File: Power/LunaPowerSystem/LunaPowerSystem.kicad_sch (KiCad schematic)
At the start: 6 parts, among them SW1 KILL_SWITCH

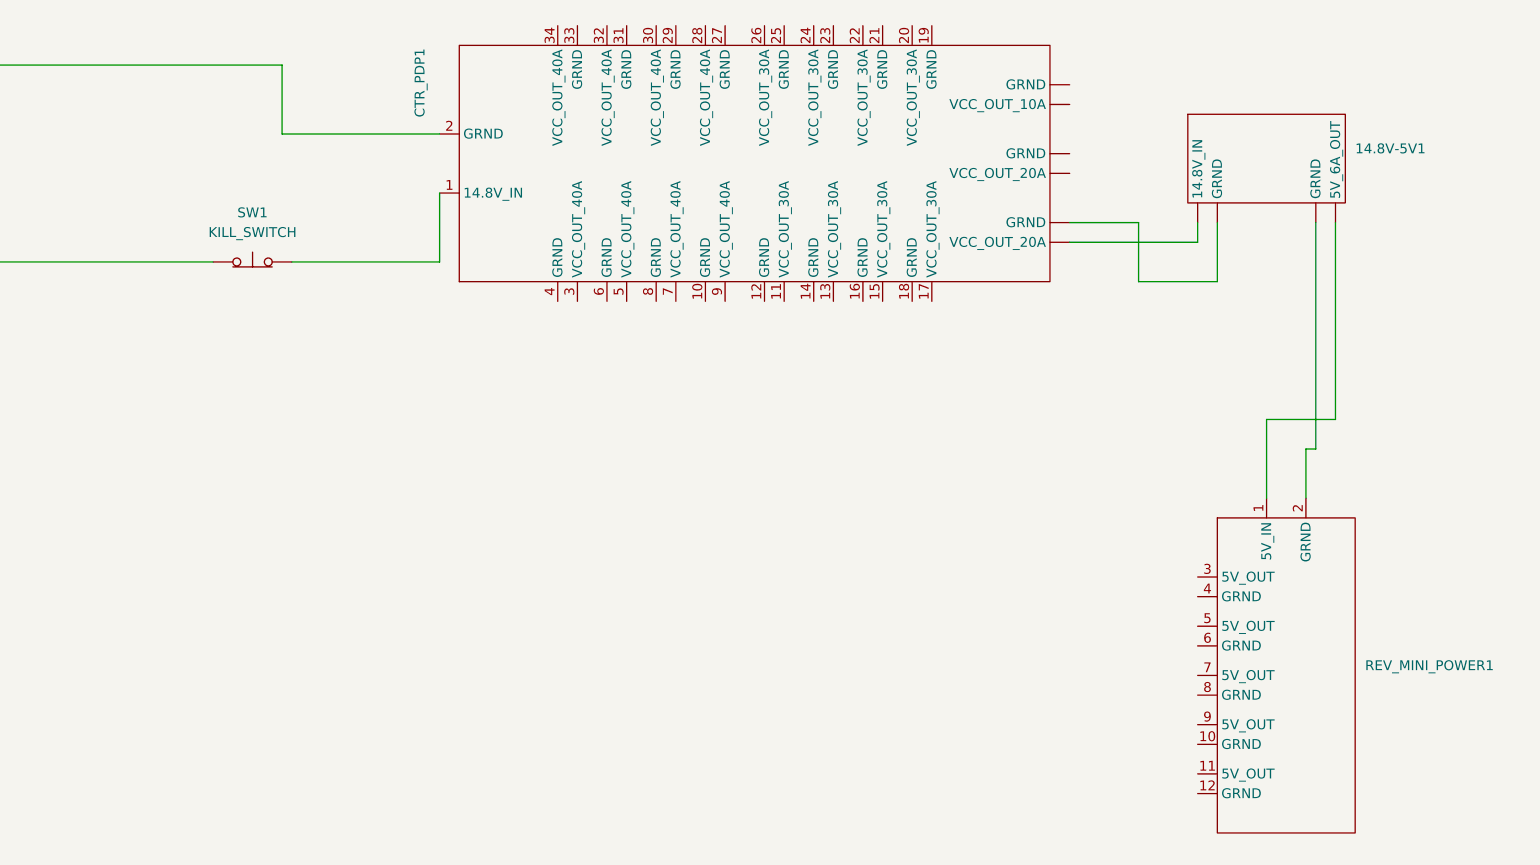
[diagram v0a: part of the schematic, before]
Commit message: Fixed things
At least my version of the mech schematic was broken, so I copied in the last version committed by Alex, and I updated the power schematic to use library symbols
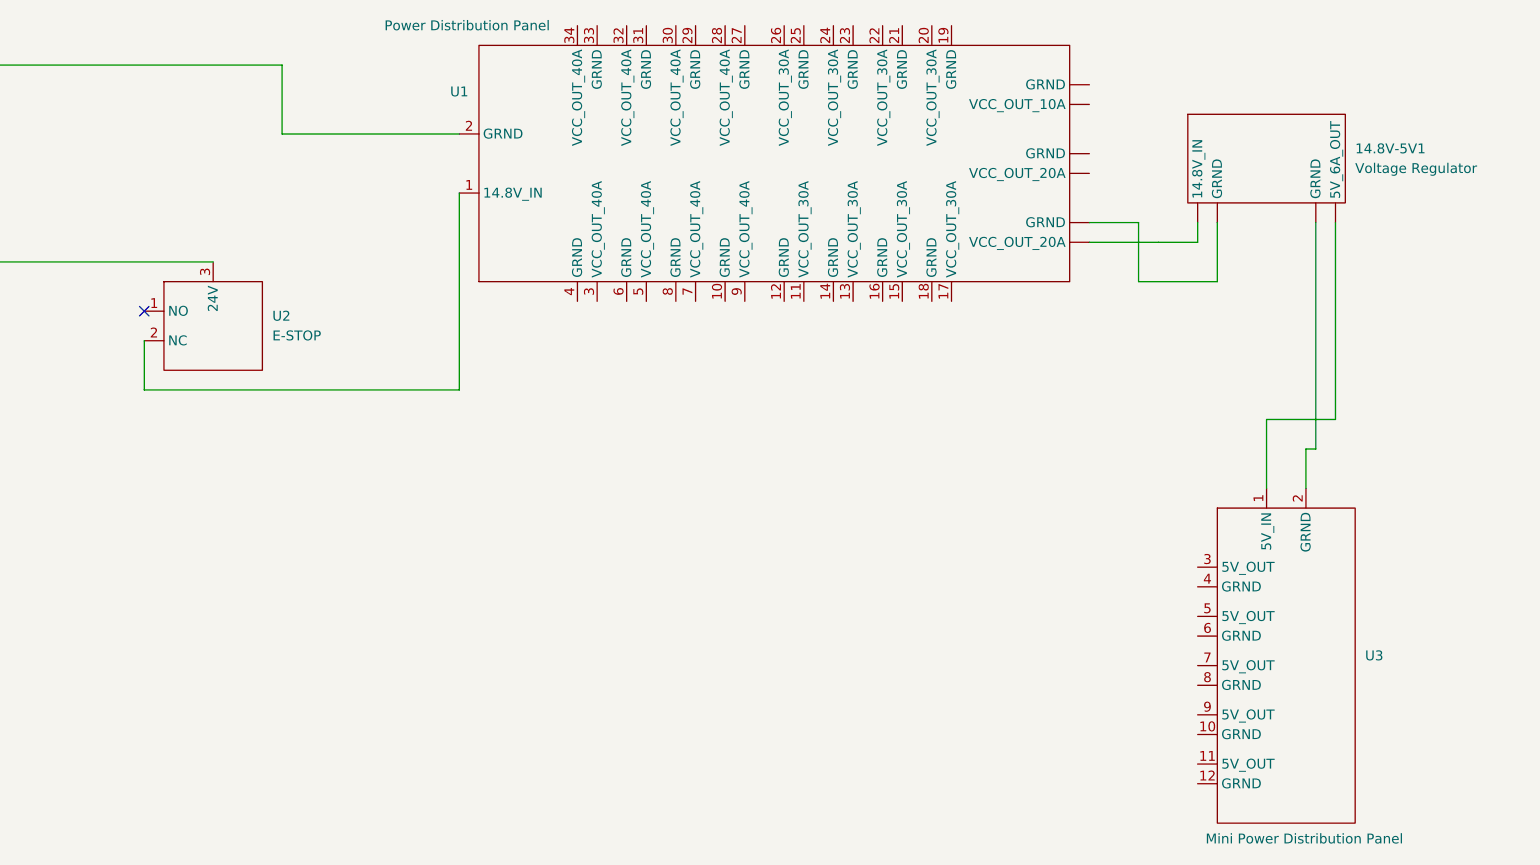
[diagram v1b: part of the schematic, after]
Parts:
- removed CTR_PDP1: ~, symbol New_Library:CTR_PDP
- removed REV_MINI_POWER1: ~, symbol New_Library:REV_Mini_Power_Module
- removed SW1: KILL_SWITCH, symbol Switch:SW_Push_Open
- added U1: Power Distribution Panel, symbol Lunabotics 2025-26:Power_Distribution_Panel
- added U2: E-STOP, symbol Lunabotics 2025-26:A22E-M-11
- added U3: Mini Power Distribution Panel, symbol Lunabotics 2025-26:Mini_Power_Distribution_Panel
- 14.8V-5V1: value ~ -> Voltage Regulator
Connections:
- net at BT1.1 (+), BT2.1 (+): now also U2.3 (24V)
- net at BT1.2 (-), BT2.2 (-): now also U1.2 (GRND)
- net at 14.8V-5V1. (5V_6A_OUT): now also U3.2 (GRND)
- new net: 14.8V-5V1. (5V_6A_OUT), U1. (GRND) (x2)
- new net: U1.1 (14.8V_IN), U2.2 (NC)
- new net: 14.8V-5V1. (5V_6A_OUT), U3.1 (5V_IN)
- no-connect marks 0 -> 1

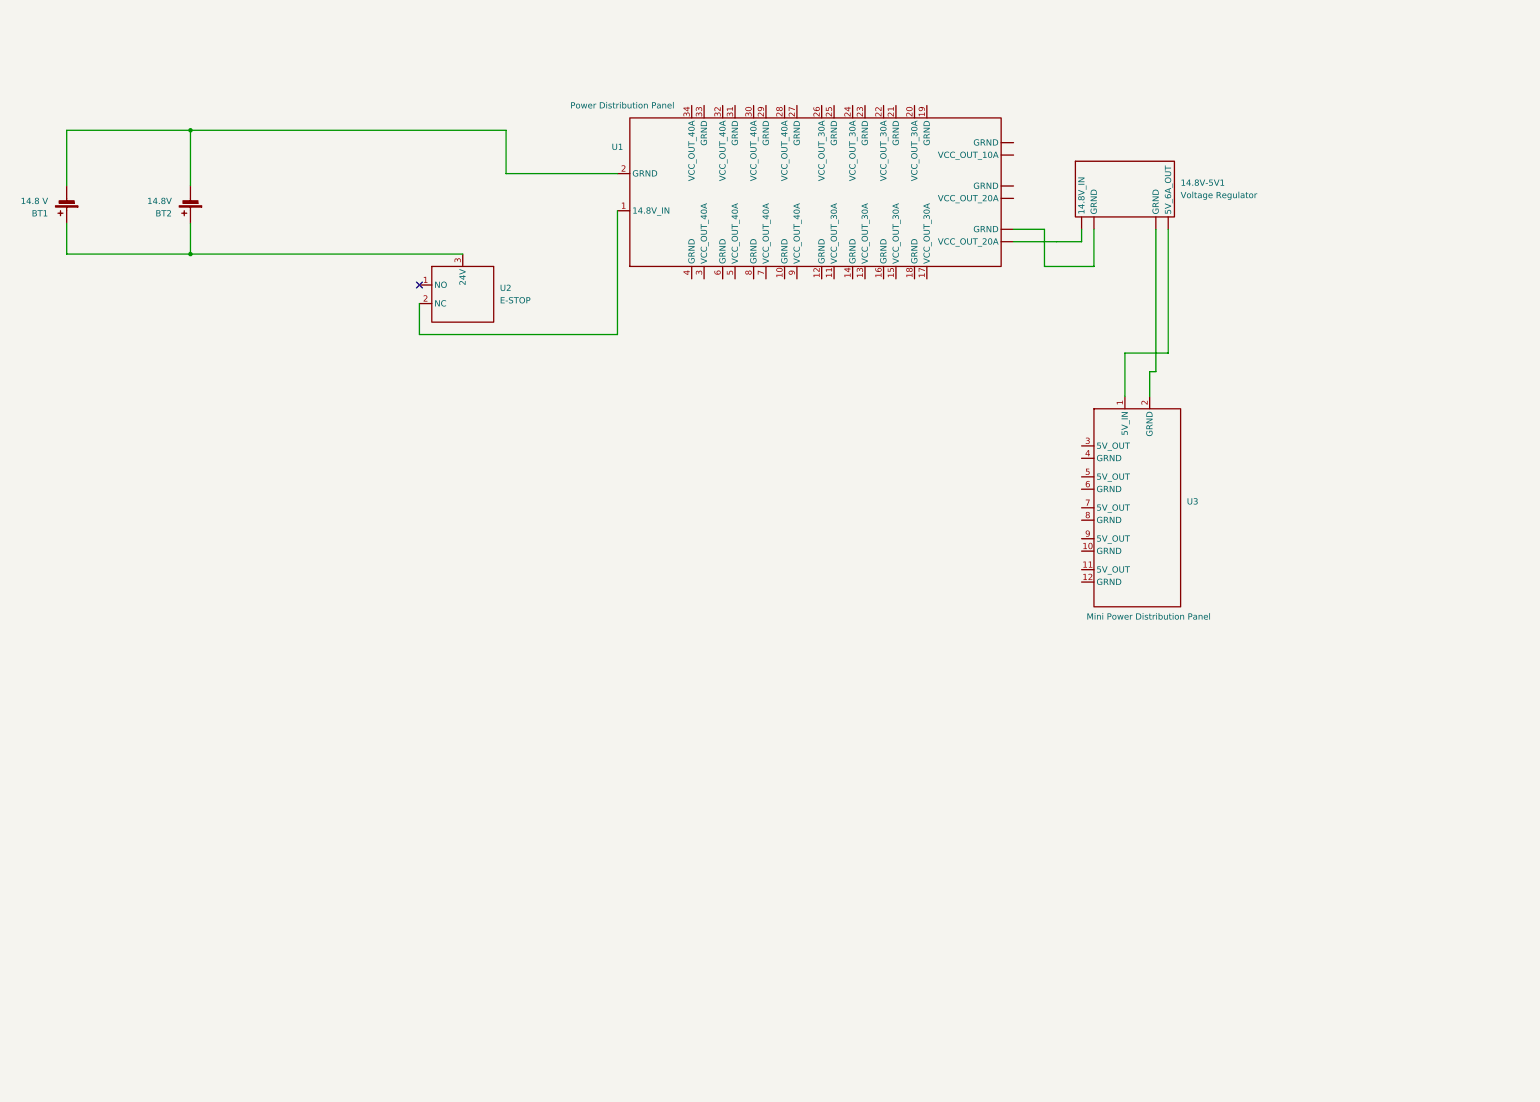
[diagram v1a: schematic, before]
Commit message: Completed Schematics
Only thing not included is a linear actuator and motor controller. Waiting on Mechanical to give us what they want to use
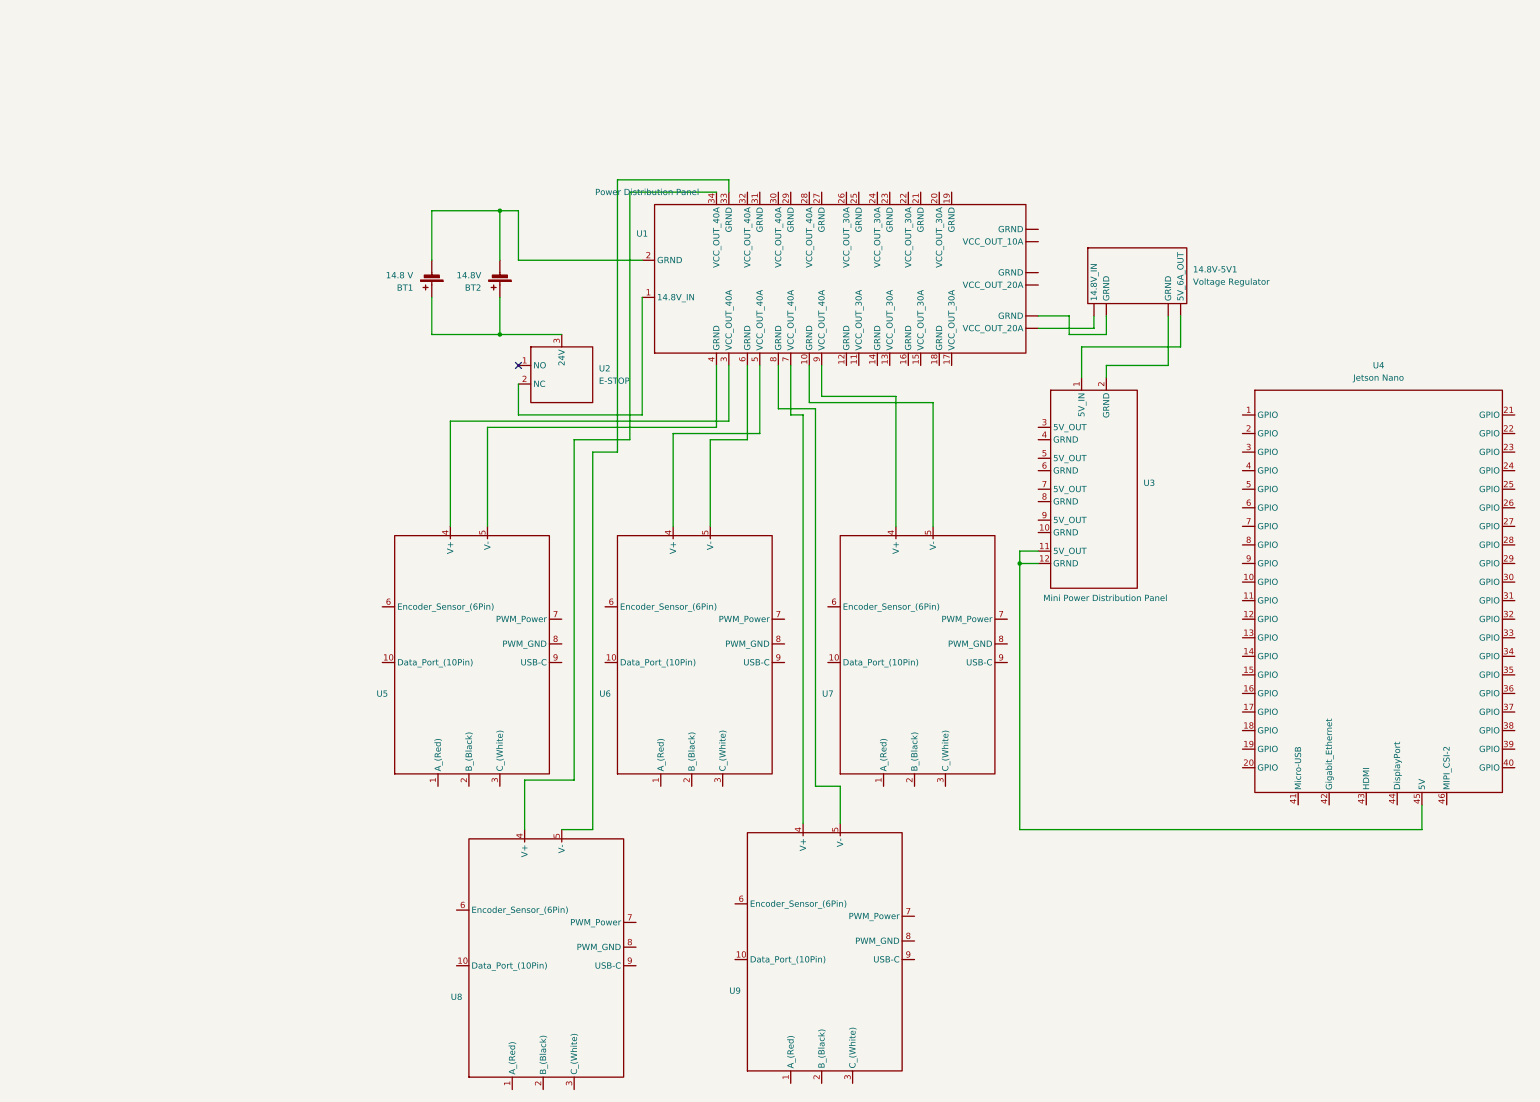
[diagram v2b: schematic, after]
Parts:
- added U4: Jetson Nano, symbol Lunabotics 2025-26:Jetson_Nano
- added U5, U6, U7, U8, U9: ~, symbol Lunabotics 2025-26:Spark_MAX_Motor_Controller
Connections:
- net at U1. (GRND): now also 14.8V-5V1. (5V_6A_OUT)
- net at 14.8V-5V1. (5V_6A_OUT): now also U3.2 (GRND); no longer U1. (GRND)
- net at U1.10 (GRND): now also U7.5 (V-)
- net at U1.3 (VCC_OUT_40A): now also U5.4 (V+)
- net at U1.33 (GRND): now also U8.5 (V-)
- net at U1.34 (VCC_OUT_40A): now also U8.4 (V+)
- net at U1.4 (GRND): now also U5.5 (V-)
- net at U1.5 (VCC_OUT_40A): now also U6.4 (V+)
- net at U1.6 (GRND): now also U6.5 (V-)
- net at U1.7 (VCC_OUT_40A): now also U9.4 (V+)
- net at U1.8 (GRND): now also U9.5 (V-)
- net at U1.9 (VCC_OUT_40A): now also U7.4 (V+)
- net at U3.11 (5V_OUT): now also U3.12 (GRND), U4.45 (5V)
- new net: 14.8V-5V1. (5V_6A_OUT), U1. (GRND)
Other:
- moved on the sheet: 14.8V-5V1, BT1, BT2, U1, U2, U3

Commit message: Power Schematic Update
Added Additional Spark MAX to Power System Schematic, updated Jetson Nano 5V barrel connector on Symbol Library, updated Jetson Nano power delivery.
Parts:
- added U10: ~, symbol Lunabotics 2025-26:Spark_MAX_Motor_Controller
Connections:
- net at U1. (GRND): now also 14.8V-5V1. (5V_6A_OUT)
- net at 14.8V-5V1. (5V_6A_OUT): now also U3.2 (GRND); no longer U1. (GRND)
- net at U1.31 (GRND): now also U10.4 (V+)
- net at U1.32 (VCC_OUT_40A): now also U10.5 (V-)
- new net: 14.8V-5V1. (5V_6A_OUT), U1. (GRND)
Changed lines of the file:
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@@
 	)
 	(junction
-		(at 229.87 128.27)
+		(at 312.42 177.8)
 		(diameter 0)
-		(color 0 0 0 1)
+		(color 0 0 0 0)
 	)
 	(no_connect
@@
 	(wire
 		(pts
+			(xy 312.42 177.8) (xy 312.42 182.88)
+		)
+		(stroke
+			(width 0)
+			(type default)
+			(color 255 0 7 1)
+		)
+	)
+	(wire
+		(pts
 			(xy 123.19 73.66) (xy 123.19 81.28)
 		)
@@
 	(wire
 		(pts
-			(xy 229.87 128.27) (xy 233.68 128.27)
+			(xy 173.99 36.83) (xy 232.41 36.83)
 		)
 		(stroke
@@
 	(wire
 		(pts
-			(xy 312.42 177.8) (xy 312.42 182.88)
-		)
-		(stroke
-			(width 0)
-			(type default)
-			(color 0 0 0 1)
-		)
-	)
-	(wire
-		(pts
 			(xy 127 55.88) (xy 127 66.04)
 		)
@@
 	(wire
 		(pts
+			(xy 232.41 184.15) (xy 313.69 184.15)
+		)
+		(stroke
+			(width 0)
+			(type default)
+			(color 0 0 0 1)
+		)
+	)
+	(wire
+		(pts
 			(xy 233.68 77.47) (xy 240.03 77.47)
 		)
@@
 	(wire
 		(pts
-			(xy 229.87 128.27) (xy 229.87 125.73)
-		)
-		(stroke
-			(width 0)
-			(type default)
-			(color 0 0 0 1)
-		)
-	)
-	(wire
-		(pts
 			(xy 247.65 87.63) (xy 247.65 90.17)
 		)
@@
 	(wire
 		(pts
+			(xy 176.53 29.21) (xy 232.41 29.21)
+		)
+		(stroke
+			(width 0)
+			(type default)
+			(color 255 0 0 1)
+		)
+	)
+	(wire
+		(pts
 			(xy 204.47 120.65) (xy 204.47 93.98)
 		)
@@
 	(wire
 		(pts
+			(xy 313.69 184.15) (xy 313.69 177.8)
+		)
+		(stroke
+			(width 0)
+			(type default)
+			(color 0 0 0 1)
+		)
+	)
+	(wire
+		(pts
 			(xy 113.03 99.06) (xy 170.18 99.06)
 		)
@@
 	(wire
 		(pts
+			(xy 173.99 52.07) (xy 173.99 36.83)
+		)
+		(stroke
+			(width 0)
+			(type default)
+			(color 0 0 0 1)
+		)
+	)
+	(wire
+		(pts
 			(xy 152.4 97.79) (xy 152.4 73.66)
 		)
@@
 	(wire
 		(pts
+			(xy 229.87 125.73) (xy 229.87 182.88)
+		)
+		(stroke
+			(width 0)
+			(type default)
+			(color 249 0 0 1)
+		)
+	)
+	(wire
+		(pts
+			(xy 233.68 128.27) (xy 232.41 128.27)
+		)
+		(stroke
+			(width 0)
+			(type default)
+			(color 0 0 0 1)
+		)
+	)
+	(wire
+		(pts
 			(xy 262.89 77.47) (xy 262.89 83.82)
 		)
@@
 	(wire
 		(pts
+			(xy 176.53 52.07) (xy 176.53 29.21)
+		)
+		(stroke
+			(width 0)
+			(type default)
+			(color 255 6 0 1)
+		)
+	)
+	(wire
+		(pts
 			(xy 187.96 173.99) (xy 187.96 96.52)
 		)
@@
 	(wire
 		(pts
+			(xy 313.69 177.8) (xy 312.42 177.8)
+		)
+		(stroke
+			(width 0)
+			(type default)
+			(color 0 0 0 1)
+		)
+	)
+	(wire
+		(pts
 			(xy 128.27 172.72) (xy 138.43 172.72)
 		)
@@
 	(wire
 		(pts
+			(xy 232.41 128.27) (xy 232.41 184.15)
+		)
+		(stroke
+			(width 0)
+			(type default)
+			(color 0 0 0 1)
+		)
+	)
+	(wire
+		(pts
 			(xy 138.43 102.87) (xy 149.86 102.87)
 		)
@@
 		(pts
 			(xy 193.04 181.61) (xy 193.04 173.99)
-		)
-		(stroke
-			(width 0)
-			(type default)
-			(color 0 0 0 1)
-		)
-	)
-	(wire
-		(pts
-			(xy 229.87 182.88) (xy 229.87 128.27)
 		)
 		(stroke
@@
 					(unit 1)
 				)
+			)
+		)
+	)
+	(symbol
+		(lib_id "Lunabotics 2025-26:Spark_MAX_Motor_Controller")
+		(at 254 33.02 270)
+		(unit 1)
+		(exclude_from_sim no)
+		(in_bom yes)
+		(on_board yes)
+		(dnp no)
+		(fields_autoplaced yes)
+		(property "Reference" "U10"
+			(at 231.14 42.2754 90)
+			(effects
+				(font
+					(size 1.27 1.27)
+				)
+			)
+		)
+		(property "Value" "~"
+			(at 231.14 39.7354 90)
+			(effects
+				(font
+					(size 1.27 1.27)
+				)
+			)
+		)
+		(property "Footprint" ""
+			(at 254 33.02 0)
+			(effects
+				(font
+					(size 1.27 1.27)
+				)
+				(hide yes)
+			)
+		)
+		(property "Datasheet" ""
+			(at 254 33.02 0)
+			(effects
+				(font
+					(size 1.27 1.27)
+				)
+				(hide yes)
+			)
+		)
+		(property "Description" ""
+			(at 254 33.02 0)
+			(effects
+				(font
+					(size 1.27 1.27)
+				)
+				(hide yes)
+			)
+		)
+		(pin "6"
+		)
+		(pin "1"
+		)
+		(pin "10"
+		)
+		(pin "7"
+		)
+		(pin "5"
+		)
+		(pin "9"
+		)
+		(pin "2"
+		)
+		(pin "3"
+		)
+		(pin "4"
+		)
+		(pin "8"
+		)
+		(instances
+			(project ""
+				(path "/ddb47dc6-db2c-4ed2-99c0-9b98c5e956b4"
+					(reference "U10")
+					(unit 1)
+				)
